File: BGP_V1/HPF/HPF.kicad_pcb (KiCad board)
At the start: 2 copper layers, 30 x 30 mm, 12 parts, among them P1 CONN_01X05, U1 OPA2170

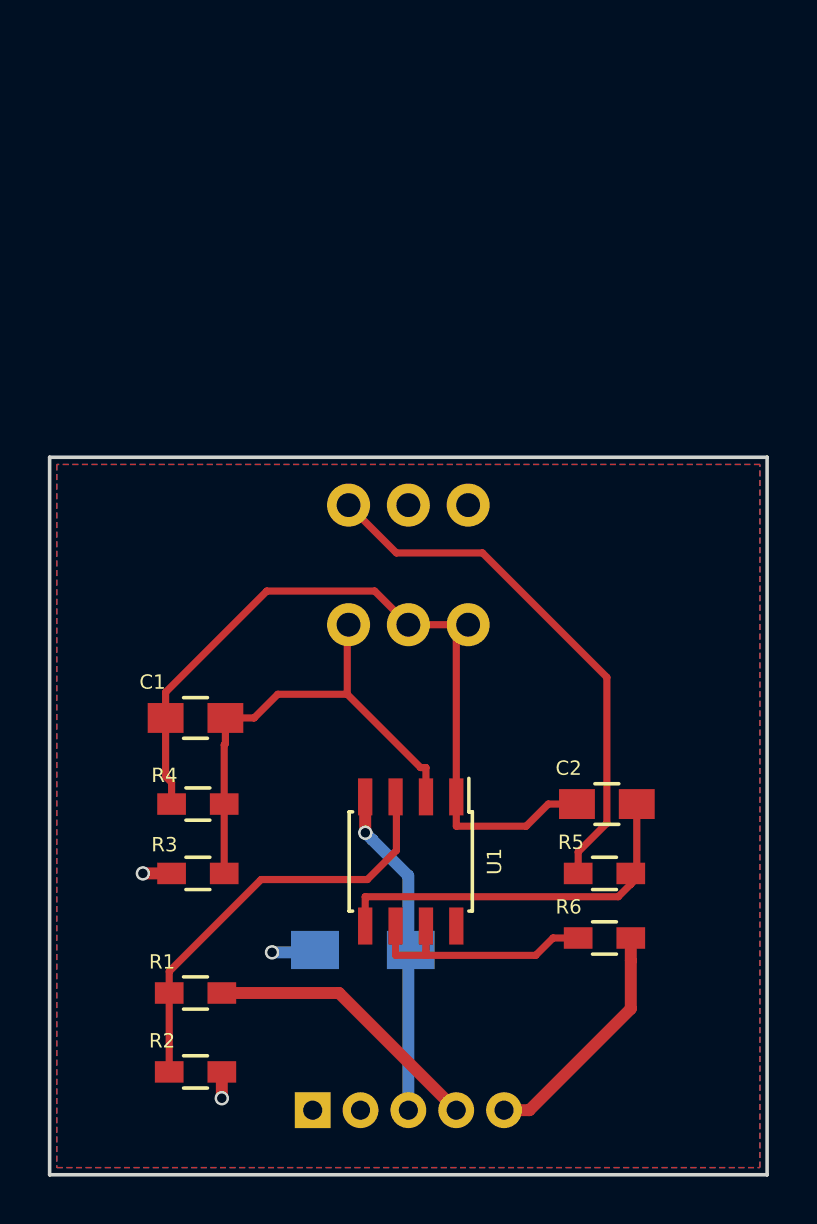
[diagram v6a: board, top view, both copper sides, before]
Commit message: Some cleanup and gerbers updated to reflect this
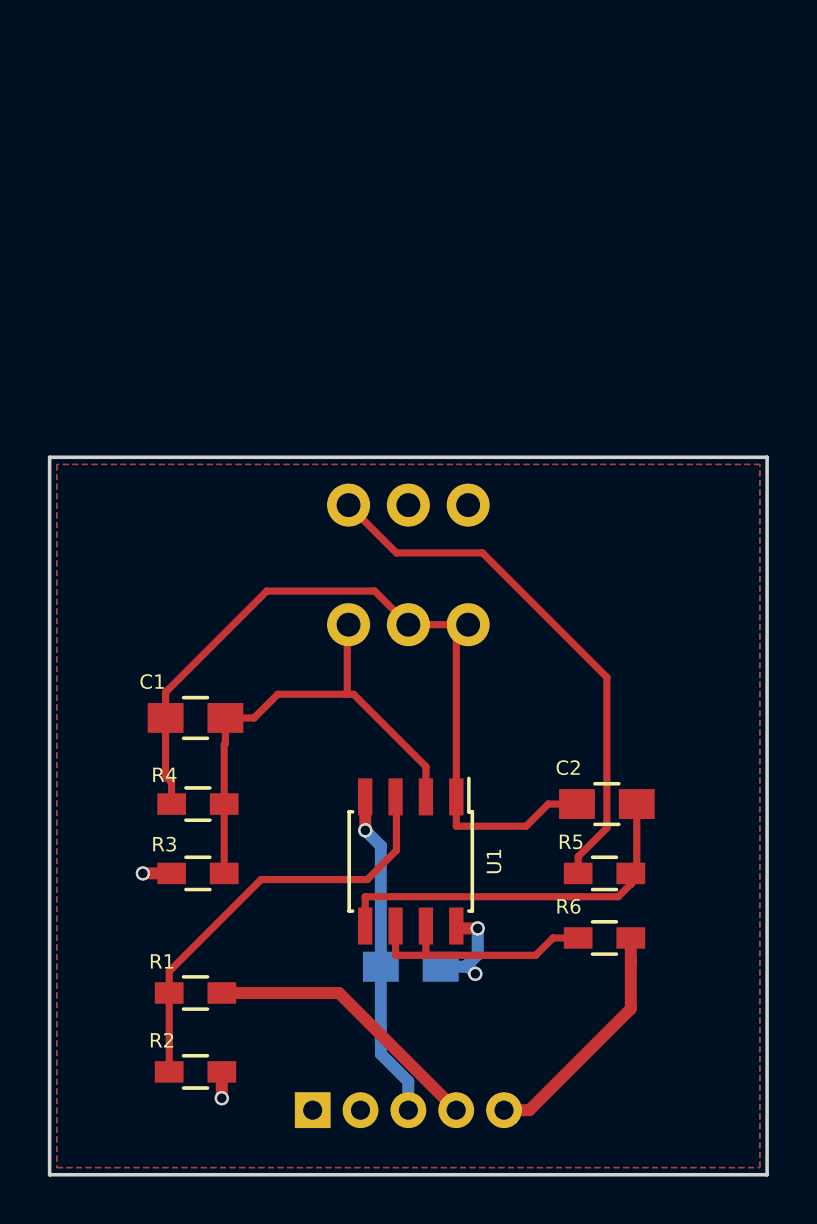
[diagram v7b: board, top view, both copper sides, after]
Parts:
- C3: footprint Capacitors_SMD:C_1206_HandSoldering -> Capacitors_SMD:C_0805_HandSoldering
- moved C3 2.12 mm to (155.1, 71.3), turned to 180 degrees
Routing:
- net /V+: track 1.70 -> 4.28 mm, vias 1 -> 2
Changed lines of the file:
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@@
     (thickness 1.6)
     (drawings 14)
-    (tracks 73)
+    (tracks 81)
     (zones 0)
     (modules 12)
@@
     )
   )
-  (module Capacitors_SMD:C_1206_HandSoldering (layer B.Cu)
-    (at 153.1 70.6)
-    (descr "Capacitor SMD 1206, hand soldering")
-    (tags "capacitor 1206")
-    (attr smd)
-    (fp_text reference C3 (at 2.8 -1.6) (layer B.SilkS)
+  (module Capacitors_SMD:C_0805_HandSoldering (layer B.Cu)
+    (at 155.1 71.3 180)
+    (descr "Capacitor SMD 0805, hand soldering")
+    (tags "capacitor 0805")
+    (attr smd)
+    (fp_text reference C3 (at -1.8 1.5 180) (layer B.SilkS)
       (effects (font (size 0.6 0.6) (thickness 0.15)) (justify mirror))
     )
-    (fp_text value 10u (at 0 -2.3) (layer B.Fab) hide
+    (fp_text value 10u (at 0 -2.1 180) (layer B.Fab) hide
       (effects (font (size 0.6 0.6) (thickness 0.15)) (justify mirror))
     )
-    (fp_line (start -3.3 1.15) (end 3.3 1.15) (layer B.CrtYd) (width 0.05))
-    (fp_line (start -3.3 -1.15) (end 3.3 -1.15) (layer B.CrtYd) (width 0.05))
-    (fp_line (start -3.3 1.15) (end -3.3 -1.15) (layer B.CrtYd) (width 0.05))
-    (fp_line (start 3.3 1.15) (end 3.3 -1.15) (layer B.CrtYd) (width 0.05))
-    (fp_line (start 1 1.025) (end -1 1.025) (layer B.SilkS) (width 0.15))
-    (fp_line (start -1 -1.025) (end 1 -1.025) (layer B.SilkS) (width 0.15))
-    (pad 1 smd rect (at -2 0) (size 2 1.6) (layers B.Cu B.Paste B.Mask)
+    (fp_line (start -2.3 1) (end 2.3 1) (layer B.CrtYd) (width 0.05))
+    (fp_line (start -2.3 -1) (end 2.3 -1) (layer B.CrtYd) (width 0.05))
+    (fp_line (start -2.3 1) (end -2.3 -1) (layer B.CrtYd) (width 0.05))
+    (fp_line (start 2.3 1) (end 2.3 -1) (layer B.CrtYd) (width 0.05))
+    (fp_line (start 0.5 0.85) (end -0.5 0.85) (layer B.SilkS) (width 0.15))
+    (fp_line (start -0.5 -0.85) (end 0.5 -0.85) (layer B.SilkS) (width 0.15))
+    (pad 1 smd rect (at -1.25 0 180) (size 1.5 1.25) (layers B.Cu B.Paste B.Mask)
       (net 4 /V+))
-    (pad 2 smd rect (at 2 0) (size 2 1.6) (layers B.Cu B.Paste B.Mask)
+    (pad 2 smd rect (at 1.25 0 180) (size 1.5 1.25) (layers B.Cu B.Paste B.Mask)
       (net 5 /V-))
-    (model Capacitors_SMD.3dshapes/C_1206_HandSoldering.wrl
+    (model Capacitors_SMD.3dshapes/C_0805_HandSoldering.wrl
       (at (xyz 0 0 0))
       (scale (xyz 1 1 1))
@@
   (segment (start 153.5937 55.5937) (end 149.081 55.5937) (width 0.3) (layer F.Cu) (net 1))
   (segment (start 155 57) (end 153.5937 55.5937) (width 0.3) (layer F.Cu) (net 1))
-  (segment (start 155.735 64.2) (end 155.735 62.9747) (width 0.3) (layer F.Cu) (net 2))
+  (segment (start 152.4446 59.9089) (end 152.7089 59.9089) (width 0.3) (layer F.Cu) (net 2))
+  (segment (start 152.7089 59.9089) (end 155.735 62.935) (width 0.3) (layer F.Cu) (net 2))
+  (segment (start 155.735 62.935) (end 155.735 62.9747) (width 0.3) (layer F.Cu) (net 2))
+  (segment (start 155.735 62.9747) (end 155.735 64.2) (width 0.3) (layer F.Cu) (net 2))
   (segment (start 152.4446 57.0554) (end 152.4446 59.9089) (width 0.3) (layer F.Cu) (net 2))
   (segment (start 152.5 57) (end 152.4446 57.0554) (width 0.3) (layer F.Cu) (net 2))
-  (segment (start 155.5104 62.9747) (end 155.735 62.9747) (width 0.3) (layer F.Cu) (net 2))
-  (segment (start 152.4446 59.9089) (end 155.5104 62.9747) (width 0.3) (layer F.Cu) (net 2))
   (segment (start 149.5414 59.9089) (end 148.5503 60.9) (width 0.3) (layer F.Cu) (net 2))
   (segment (start 152.4446 59.9089) (end 149.5414 59.9089) (width 0.3) (layer F.Cu) (net 2))
@@
   (segment (start 153.195 68.3747) (end 163.7754 68.3747) (width 0.3) (layer F.Cu) (net 3))
   (segment (start 153.195 69.6) (end 153.195 68.3747) (width 0.3) (layer F.Cu) (net 3))
-  (segment (start 151 70.7) (end 149.300004 70.7) (width 0.5) (layer B.Cu) (net 4))
-  (via (at 149.300004 70.7) (size 0.6) (drill 0.4) (layers F.Cu B.Cu) (net 4))
-  (segment (start 155 77.3) (end 155 70.7) (width 0.5) (layer B.Cu) (net 5))
-  (segment (start 155 70.7) (end 155.1 70.6) (width 0.5) (layer B.Cu) (net 5))
-  (segment (start 153.499999 65.999999) (end 153.2 65.7) (width 0.5) (layer B.Cu) (net 5))
-  (segment (start 155 70.7) (end 155 67.5) (width 0.5) (layer B.Cu) (net 5))
-  (segment (start 153.195 65.695) (end 153.2 65.7) (width 0.5) (layer F.Cu) (net 5))
-  (segment (start 155 67.5) (end 153.499999 65.999999) (width 0.5) (layer B.Cu) (net 5))
-  (segment (start 153.195 64.2) (end 153.195 65.695) (width 0.5) (layer F.Cu) (net 5))
-  (via (at 153.2 65.7) (size 0.6) (drill 0.4) (layers F.Cu B.Cu) (net 5))
+  (segment (start 157.9 69.7) (end 157.105 69.7) (width 0.5) (layer F.Cu) (net 4))
+  (segment (start 157.105 69.7) (end 157.005 69.6) (width 0.5) (layer F.Cu) (net 4))
+  (segment (start 157.5 71.2) (end 157.9 70.8) (width 0.5) (layer B.Cu) (net 4))
+  (segment (start 157.9 70.8) (end 157.9 69.7) (width 0.5) (layer B.Cu) (net 4))
+  (via (at 157.9 69.7) (size 0.6) (drill 0.4) (layers F.Cu B.Cu) (net 4))
+  (segment (start 157.5 71.3) (end 157.5 71.2) (width 0.5) (layer B.Cu) (net 4))
+  (segment (start 156.35 71.3) (end 157.5 71.3) (width 0.5) (layer B.Cu) (net 4))
+  (segment (start 157.5 71.3) (end 157.8 71.6) (width 0.5) (layer B.Cu) (net 4))
+  (via (at 157.8 71.6) (size 0.6) (drill 0.4) (layers F.Cu B.Cu) (net 4))
+  (segment (start 153.2 65.6) (end 153.2 64.205) (width 0.5) (layer F.Cu) (net 5))
+  (segment (start 153.2 64.205) (end 153.195 64.2) (width 0.5) (layer F.Cu) (net 5))
+  (segment (start 153.85 71.3) (end 153.85 66.25) (width 0.5) (layer B.Cu) (net 5))
+  (segment (start 153.85 66.25) (end 153.2 65.6) (width 0.5) (layer B.Cu) (net 5))
+  (via (at 153.2 65.6) (size 0.6) (drill 0.4) (layers F.Cu B.Cu) (net 5))
+  (segment (start 155 76.1) (end 153.85 74.95) (width 0.5) (layer B.Cu) (net 5))
+  (segment (start 153.85 74.95) (end 153.85 71.3) (width 0.5) (layer B.Cu) (net 5))
+  (segment (start 155 77.3) (end 155 76.1) (width 0.5) (layer B.Cu) (net 5))
   (segment (start 147.2 76.799996) (end 147.199996 76.8) (width 0.5) (layer F.Cu) (net 6))
   (segment (start 147.2 75.7) (end 147.2 76.799996) (width 0.5) (layer F.Cu) (net 6))
@@
   (segment (start 145 71.4997) (end 145 72.4) (width 0.3) (layer F.Cu) (net 9))
   (segment (start 145 75.7) (end 145 72.4) (width 0.3) (layer F.Cu) (net 9))
-  (segment (start 162.1 67.4) (end 162.1 66.4997) (width 0.3) (layer F.Cu) (net 10))
-  (segment (start 162.1 66.4997) (end 163.3 65.2997) (width 0.3) (layer F.Cu) (net 10))
-  (segment (start 163.3 65.2997) (end 163.3 59.2) (width 0.3) (layer F.Cu) (net 10))
+  (segment (start 162.1 67.4) (end 162.1 66.7) (width 0.3) (layer F.Cu) (net 10))
+  (segment (start 162.1 66.7) (end 163.3 65.5) (width 0.3) (layer F.Cu) (net 10))
   (segment (start 163.3 59.2) (end 158.1 54) (width 0.3) (layer F.Cu) (net 10))
+  (segment (start 163.3 65.5) (end 163.3 59.2) (width 0.3) (layer F.Cu) (net 10))
   (segment (start 158.1 54) (end 154.5 54) (width 0.3) (layer F.Cu) (net 10))
   (segment (start 154.5 54) (end 152.5 52) (width 0.3) (layer F.Cu) (net 10))

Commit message: Changed 1_HPF to use ALPHA 12mm pot.
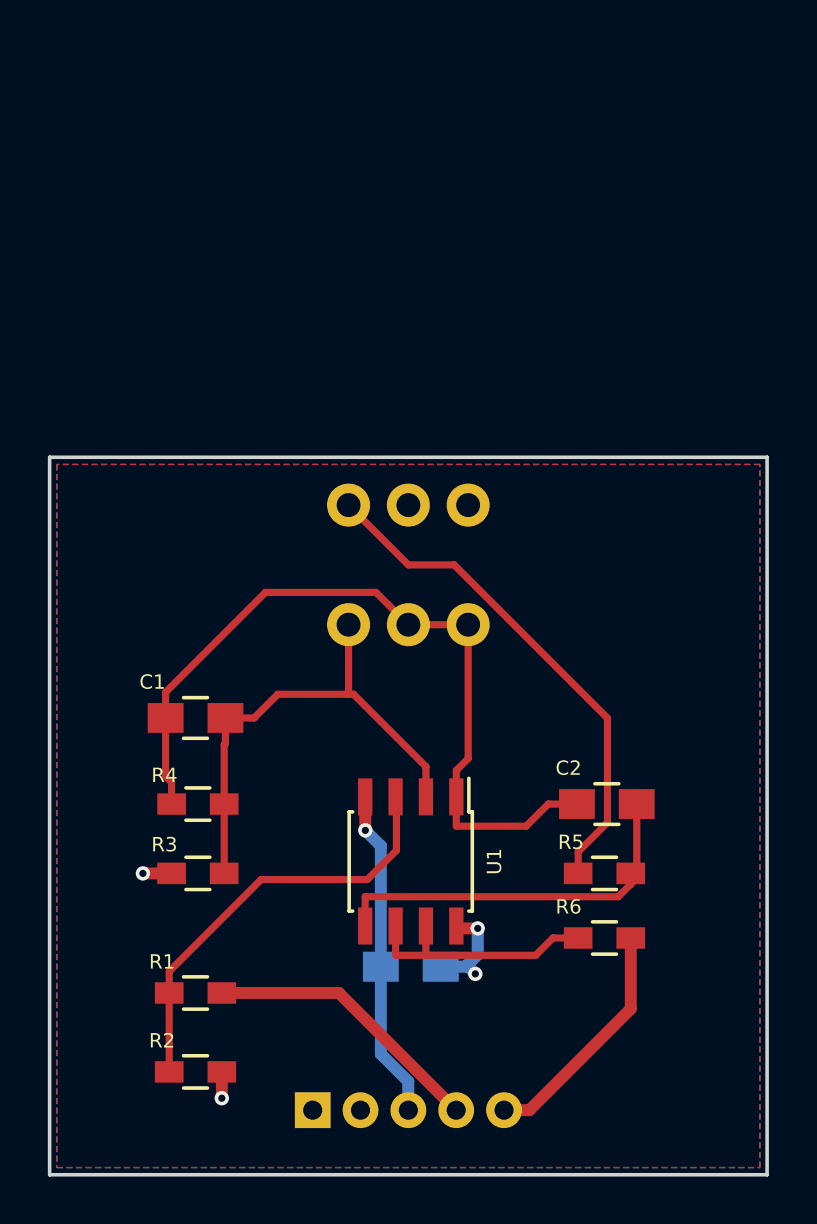
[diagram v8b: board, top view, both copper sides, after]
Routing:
- net /VF_1: track 22.5 -> 21.5 mm
